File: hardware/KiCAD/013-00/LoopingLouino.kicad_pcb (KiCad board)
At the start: 2 copper layers, 50 x 30 mm, 62 parts, among them CON1 BARREL_JACK_reduced, CON2 AVR-ISP-6, IC1 ATMEGA328P-A, J1 JACK_4P, P1 CONN_01X04, P2 CONN_01X03, P3 CONN_01X02, P4 CONN_01X01, P5 CONN_01X01, Q1 Q_PMOS_GSD, Q4 BCR141, Q5 BCR141, SW1 SW_PUSH, SW2 SW_PUSH, U2 MP1584, U3 ZXMHC6A07T8-2

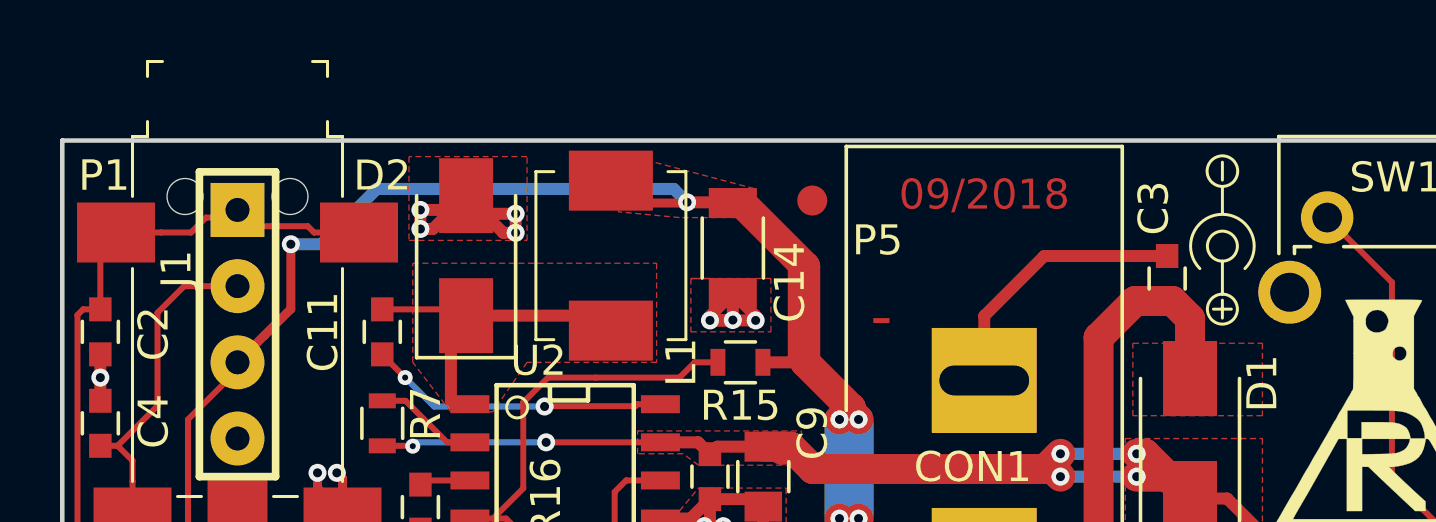
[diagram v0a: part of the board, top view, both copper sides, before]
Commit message: add new KiCAD files
add information on how to flash the bootloader
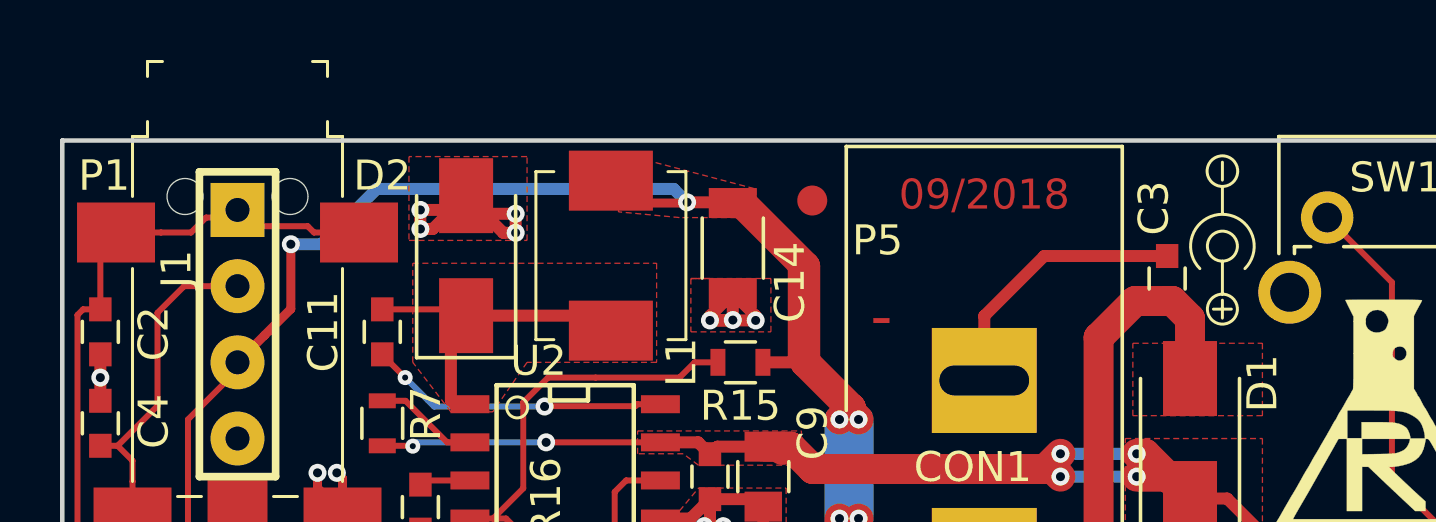
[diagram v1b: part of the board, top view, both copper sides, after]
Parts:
- C1: value C -> 1n
- C12: value 220p -> 100p
- C14: value 22u -> 22u/16V
- C16, C9: value 10u/50V -> 1u/25V
- C17, C18: value 1n -> 100n
- C19: value C_Small -> 100n
- C3: value 100n/100V -> 1n/100V
- C7: value 33n -> 100n
- P1: value CONN_01X04 -> *CONN_01X04
- Q1: value Q_PMOS_GSD -> *Q_PMOS_GSD
- R10: value 4k7 -> 0R
- R11: value 33 -> *33R
- R12: value 68k1 -> 100k
- R13, R18, R20: value R_Small -> 10k
- R15: value 50k -> 39k
- R16: value 40k -> 7k5
- R17: value R -> 2R2
- R2: value R_Small -> 22k
- R21, R22: value 100k -> 1k
- R23, R24: value 100k -> 22k
- R25: value 1k -> *1k
- R3: value R_Small -> 1k
- R4: value R_Small -> *0R
- R5: value 10k -> *10k
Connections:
- IC1 pad 11: Net-(IC1-Pad11) -> unconnected-(IC1-Pad11)
- IC1 pad 12: Net-(IC1-Pad12) -> unconnected-(IC1-Pad12)
- IC1 pad 19: Net-(IC1-Pad19) -> unconnected-(IC1-Pad19)
- IC1 pad 22: Net-(IC1-Pad22) -> unconnected-(IC1-Pad22)
- IC1 pad 7: Net-(IC1-Pad7) -> unconnected-(IC1-Pad7)
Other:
- net class Default removed
